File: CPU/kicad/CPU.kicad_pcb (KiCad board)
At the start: 6 copper layers, 4 parts, among them IC1 71256SA20TPGI, J1 Conn_02x20_Odd_Even, U1 W65C02SxP, U2 74HC00

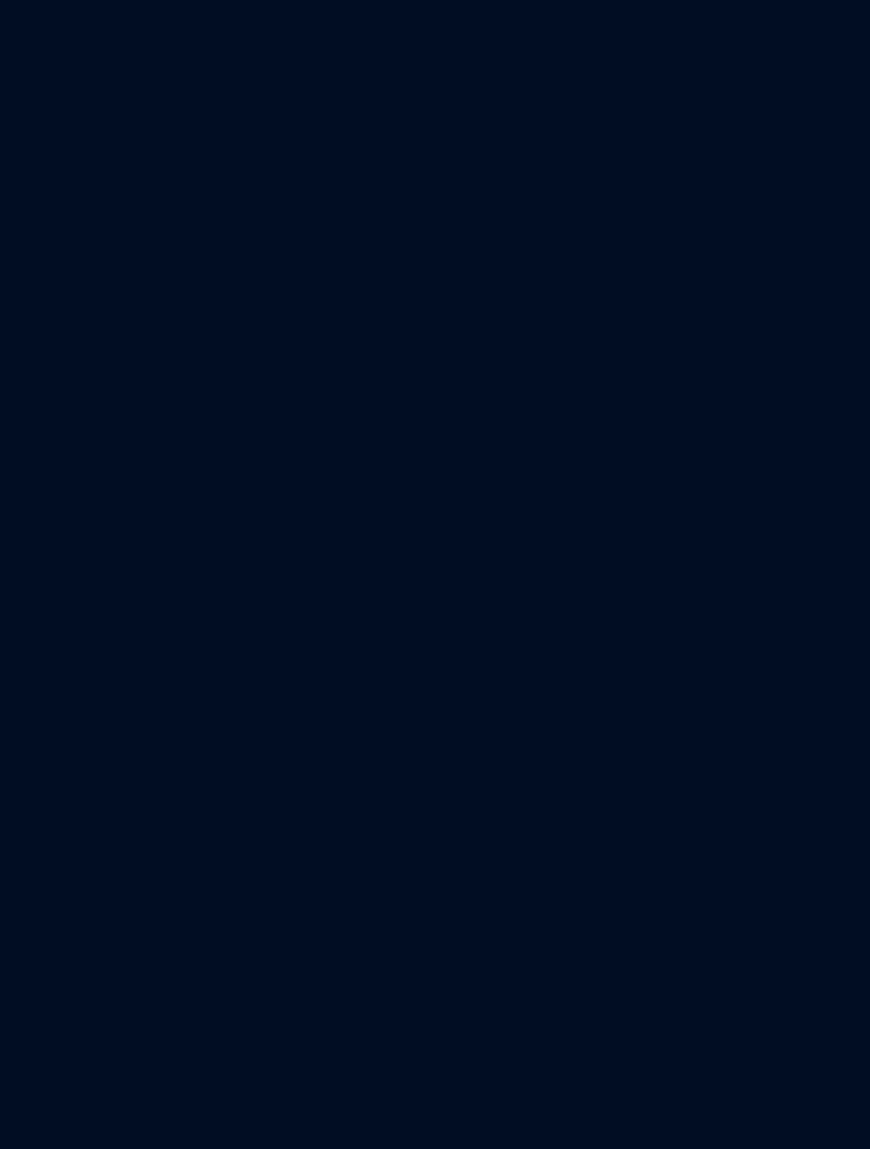
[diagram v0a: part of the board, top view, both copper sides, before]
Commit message: add oscillator, extend memory map
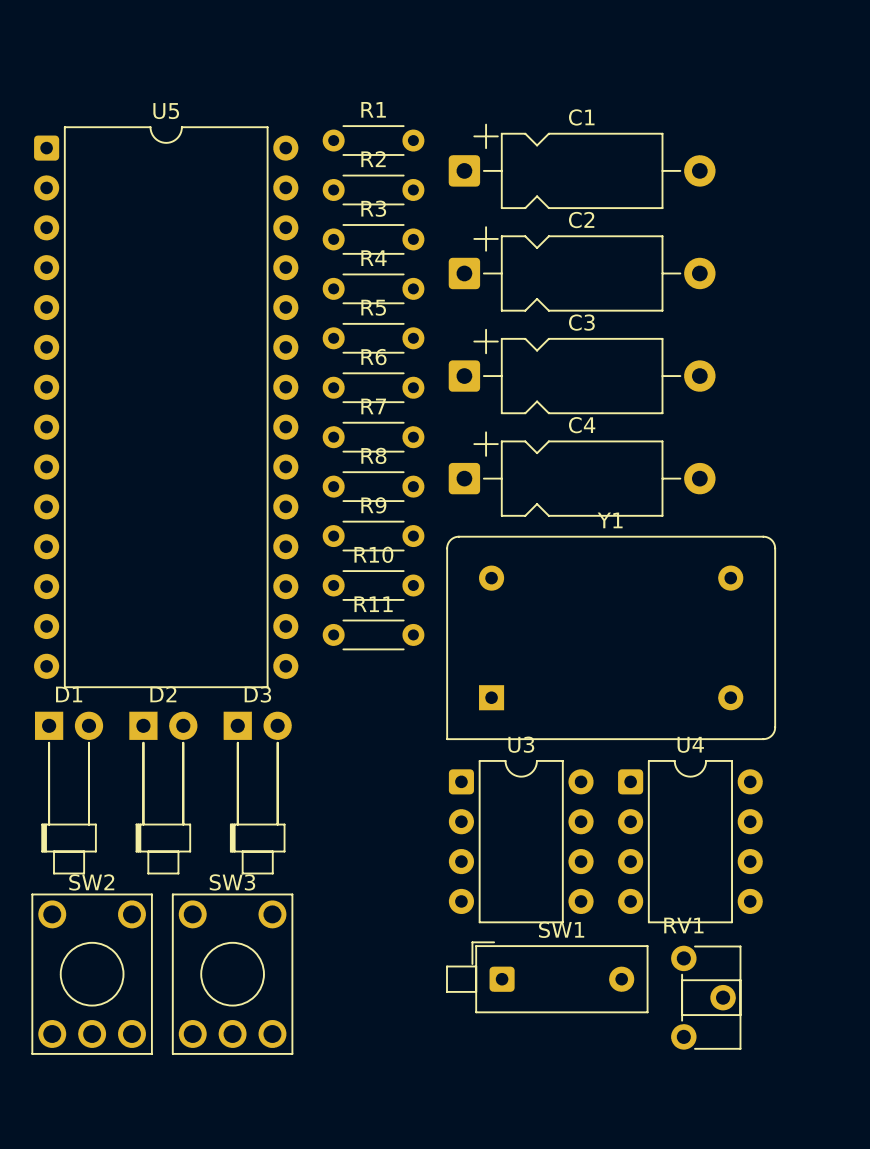
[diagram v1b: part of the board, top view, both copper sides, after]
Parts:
- added C1: 10uF, Capacitor_THT:CP_Axial_L10.0mm_D4.5mm_P15.00mm_Horizontal, F.Cu at (123.8, 90.0)
- added C2: 103, Capacitor_THT:CP_Axial_L10.0mm_D4.5mm_P15.00mm_Horizontal, F.Cu at (123.8, 96.5)
- added C3: 10uF, Capacitor_THT:CP_Axial_L10.0mm_D4.5mm_P15.00mm_Horizontal, F.Cu at (123.8, 103.0)
- added C4: 103, Capacitor_THT:CP_Axial_L10.0mm_D4.5mm_P15.00mm_Horizontal, F.Cu at (123.8, 109.6)
- added D1: Yellow, LED_THT:LED_D1.8mm_W1.8mm_H2.4mm_Horizontal_O6.35mm_Z1.6mm, F.Cu at (97.3, 125.3)
- added D2: Red, LED_THT:LED_D1.8mm_W1.8mm_H2.4mm_Horizontal_O6.35mm_Z1.6mm, F.Cu at (103.3, 125.3)
- added D3: Blue, LED_THT:LED_D1.8mm_W1.8mm_H2.4mm_Horizontal_O6.35mm_Z1.6mm, F.Cu at (109.3, 125.3)
- added R1: 220, Resistor_THT:R_Axial_DIN0204_L3.6mm_D1.6mm_P5.08mm_Horizontal, F.Cu at (115.5, 88.0)
- added R10: 1m, Resistor_THT:R_Axial_DIN0204_L3.6mm_D1.6mm_P5.08mm_Horizontal, F.Cu at (115.5, 116.4)
- added R11: 10k, Resistor_THT:R_Axial_DIN0204_L3.6mm_D1.6mm_P5.08mm_Horizontal, F.Cu at (115.5, 119.5)
- added R2: 1k, Resistor_THT:R_Axial_DIN0204_L3.6mm_D1.6mm_P5.08mm_Horizontal, F.Cu at (115.5, 91.2)
- added R3: 1k, Resistor_THT:R_Axial_DIN0204_L3.6mm_D1.6mm_P5.08mm_Horizontal, F.Cu at (115.5, 94.3)
- added R4: 1k, Resistor_THT:R_Axial_DIN0204_L3.6mm_D1.6mm_P5.08mm_Horizontal, F.Cu at (115.5, 97.5)
- added R5: 1k, Resistor_THT:R_Axial_DIN0204_L3.6mm_D1.6mm_P5.08mm_Horizontal, F.Cu at (115.5, 100.6)
- added R6: 1k, Resistor_THT:R_Axial_DIN0204_L3.6mm_D1.6mm_P5.08mm_Horizontal, F.Cu at (115.5, 103.8)
- added R7: 1k, Resistor_THT:R_Axial_DIN0204_L3.6mm_D1.6mm_P5.08mm_Horizontal, F.Cu at (115.5, 106.9)
- added R8: 1k, Resistor_THT:R_Axial_DIN0204_L3.6mm_D1.6mm_P5.08mm_Horizontal, F.Cu at (115.5, 110.1)
- added R9: 1k, Resistor_THT:R_Axial_DIN0204_L3.6mm_D1.6mm_P5.08mm_Horizontal, F.Cu at (115.5, 113.2)
- added RV1: 1M, Potentiometer_THT:Potentiometer_ACP_CA6-H2,5_Horizontal, F.Cu at (137.8, 140.1)
- added SW1: SW_DIP_x03, Button_Switch_THT:SW_DIP_SPSTx01_Piano_10.8x4.1mm_W7.62mm_P2.54mm, F.Cu at (126.2, 141.5)
- added SW2: step, Button_Switch_THT:KSA_Tactile_SPST, F.Cu at (97.5, 137.3)
- added SW3: reset, Button_Switch_THT:KSA_Tactile_SPST, F.Cu at (106.5, 137.3)
- added U3: NE555P, Package_DIP:DIP-8_W7.62mm, F.Cu at (123.6, 128.9)
- added U4: NE555P, Package_DIP:DIP-8_W7.62mm, F.Cu at (134.4, 128.9)
- added U5: 71256SA20TPGI, Package_DIP:DIP-28_W15.24mm, F.Cu at (97.2, 88.5)
- added Y1: 1 MHz, Oscillator:Oscillator_DIP-14, F.Cu at (125.5, 123.5)
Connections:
- J1 pad 17: /R/W -> /RWb
- J1 pad 33: unconnected-(J1-Pad33) -> +5V
- J1 pad 34: unconnected-(J1-Pad34) -> +5V
- J1 pad 37: unconnected-(J1-Pad37) -> /phi0
- J1 pad 39: unconnected-(J1-Pad39) -> GND
- J1 pad 40: unconnected-(J1-Pad40) -> GND
- U1 pad 2: unconnected-(U1-Pad2) -> Net-(U1-RDY)
- U1 pad 21: unconnected-(U1-Pad21) -> GND
- U1 pad 34: /R/W -> /RWb
- U1 pad 36: unconnected-(U1-Pad36) -> +5V
- U1 pad 37: unconnected-(U1-Pad37) -> /phi0
- U1 pad 38: unconnected-(U1-Pad38) -> +5V
- U1 pad 8: unconnected-(U1-Pad8) -> +5V
- U2 pad 10: unconnected-(U2-Pad10) -> Net-(SW1-Pad4)
- U2 pad 14: unconnected-(U2-Pad14) -> +5V
- U2 pad 6: Net-(IC1-Pad20) -> Net-(U5-~{CS})
- U2 pad 7: unconnected-(U2-Pad7) -> GND
- U2 pad 8: unconnected-(U2-Pad8) -> /phi0
- U2 pad 9: unconnected-(U2-Pad9) -> Net-(SW1-Pad4)
